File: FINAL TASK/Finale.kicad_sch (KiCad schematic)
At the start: 32 parts, among them J1 SWD Header, P1 USB_C_Plug, SW1 RESET, SW2 BOOT, U1 STM32F103C8T6, U2 AS5048B, U3 AS5048B, U4 AS5048B, U5 AS5048B, U6 AMS1117-3.3, Y1 Crystal

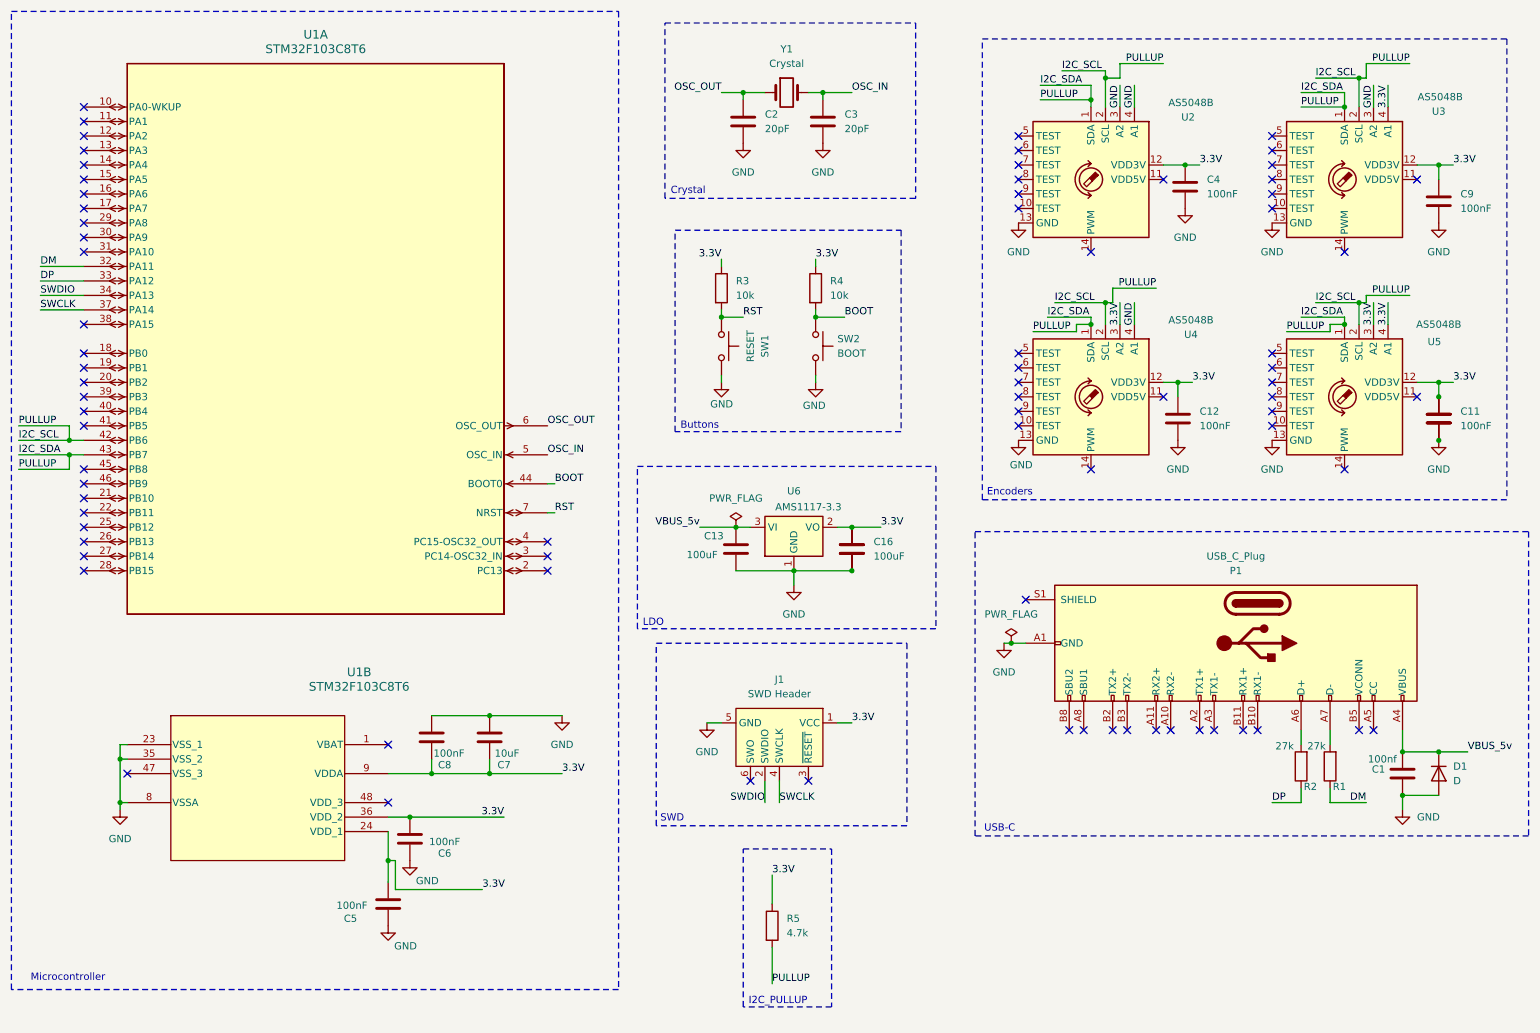
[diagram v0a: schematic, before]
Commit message: Added working directory
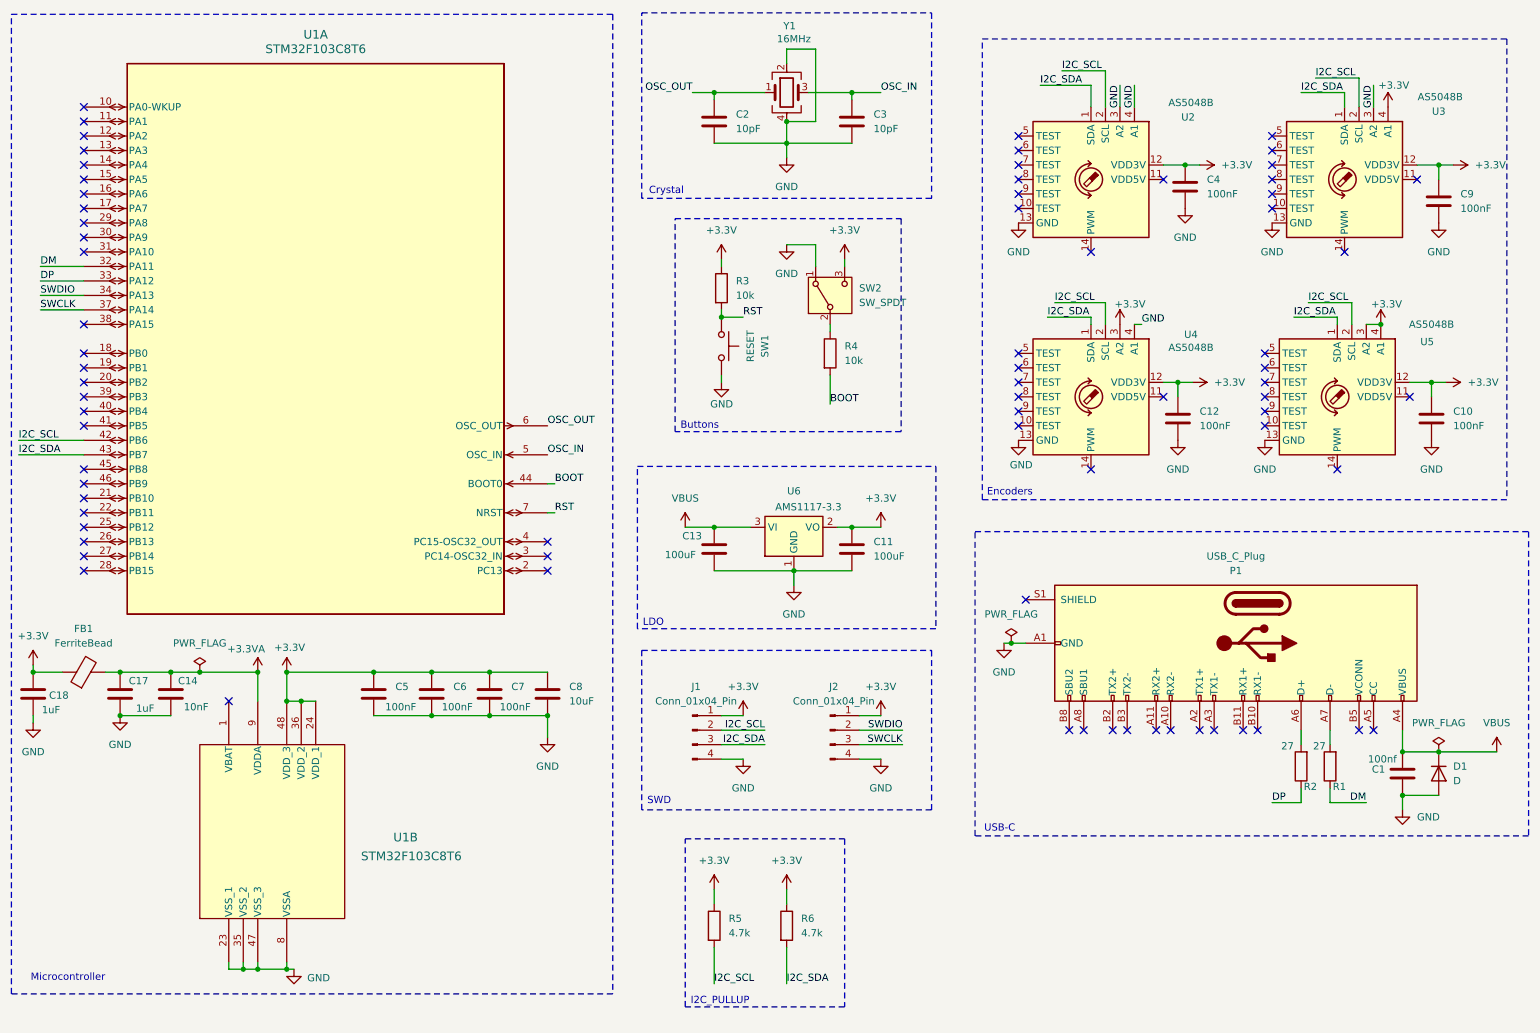
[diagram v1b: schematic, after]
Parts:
- removed C15: 100uF, Capacitor_SMD:C_0805_2012Metric, symbol Device:C
- removed C16: C, Capacitor_SMD:C_0805_2012Metric, symbol Device:C
- removed J1: SWD Header, Connector:Tag-Connect_TC2030-IDC-NL_2x03_P1.27mm_Vertical, symbol Connector:Conn_ARM_SWD_TagConnect_TC2030-NL
- removed SW2: BOOT, Button_Switch_SMD:SW_Push_SPST_NO_Alps_SKRK, symbol Switch:SW_Push
- removed Y1: Crystal, symbol Device:Crystal
- added C14: 10nF, Capacitor_SMD:C_0402_1005Metric, symbol Device:C
- added C17, C18: 1uF, Capacitor_SMD:C_0402_1005Metric, symbol Device:C
- added FB1: FerriteBead, Inductor_SMD:L_0805_2012Metric, symbol Device:FerriteBead
- added J1, J2: Conn_01x04_Pin, Connector_JST:JST_VH_B4P-VH-FB-B_1x04_P3.96mm_Vertical, symbol Connector:Conn_01x04_Pin
- added R6: 4.7k, Resistor_SMD:R_0805_2012Metric, symbol Device:R
- added SW2: SW_SPDT, Button_Switch_SMD:SW_SPDT_CK_JS102011SAQN, symbol Switch:SW_SPDT
- added Y1: 16MHz, Crystal:Crystal_SMD_3225-4Pin_3.2x2.5mm, symbol Device:Crystal_GND24
- C10: value C -> 100nF
- C11: value 100nF -> 100uF
- C2, C3: value 20pF -> 10pF; footprint Capacitor_SMD:C_0805_2012Metric -> Capacitor_SMD:C_0402_1005Metric
- C4, C5, C6: footprint Capacitor_SMD:C_0805_2012Metric -> Capacitor_SMD:C_0402_1005Metric
- C7: value 10uF -> 100nF; footprint Capacitor_SMD:C_0805_2012Metric -> Capacitor_SMD:C_0402_1005Metric
- C8: value 100nF -> 10uF
- R1, R2: value 27k -> 27
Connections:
- net GND: now also C5.2, C6.2, C7.2, C8.2, U1.47 (VSS_3), C14.2, C17.2, C18.2, J1.4 (Pin_4), J2.4 (Pin_4), SW2.1 (A), Y1.2, Y1.4; no longer C5.1, C6.1, C7.1, C8.1
- net I2C_SCL: now also J1.2 (Pin_2); no longer U1.43 (PB7), U2.1 (SDA), U3.1 (SDA), U4.1 (SDA), U5.1 (SDA)
- net OSC_IN: now also Y1.3
- net OSC_OUT: now also Y1.1
- net SWCLK: now also J2.3 (Pin_3)
- net SWDIO: now also J2.2 (Pin_2)
- net +3.3V: now reaches U1.48 (VDD_3)
- net +3.3V: now also C10.1, C11.1, C12.1, C4.1, C5.1, C6.1, C7.1, C8.1, C9.1, R3.1, R5.1, U1.24 (VDD_1), U1.36 (VDD_2), U2.12 (VDD3V), U3.12 (VDD3V), U3.4 (A1), U4.12 (VDD3V), U4.3 (A2), U5.12 (VDD3V), U5.3 (A2), U5.4 (A1), U6.2 (VO), C18.1, FB1.1, J1.1 (Pin_1), J2.1 (Pin_1), R6.1, SW2.3 (C)
- removed net 3.3V: C10.1, C11.1, C12.1, C4.1, C5.2, C6.2, C7.2, C8.2, C9.1, R3.1, R4.1, R5.1, U1.24 (VDD_1), U1.36 (VDD_2), U1.9 (VDDA), U2.12 (VDD3V), U3.12 (VDD3V), U3.4 (A1), U4.12 (VDD3V), U4.3 (A2), U5.12 (VDD3V), U5.3 (A2), U5.4 (A1), U6.2 (VO)
- net VBUS_5v renamed VBUS
- new net: R4.1, SW2.2 (B)
- new net +3.3VA: C14.1, C17.1, FB1.2, U1.9 (VDDA)
- new net I2C_SDA: J1.3 (Pin_3), R6.2, U1.43 (PB7), U2.1 (SDA), U3.1 (SDA), U4.1 (SDA), U5.1 (SDA)
- no-connect marks 79 -> 75
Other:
- moved on the sheet: C13, C2, C3, R4, R5, U1B, U5

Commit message: C
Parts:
- removed C17, C18: 1uF, Capacitor_SMD:C_0402_1005Metric, symbol Device:C
- removed D1: D, Diode_SMD:D_0805_2012Metric, symbol Device:D
- removed FB1: FerriteBead, Inductor_SMD:L_0805_2012Metric, symbol Device:FerriteBead
- removed R1, R2: 27, Resistor_SMD:R_0805_2012Metric, symbol Device:R
- added C15: 100nF, Capacitor_SMD:C_0402_1005Metric, symbol Device:C
- C10, C11, C12, C13, C9: footprint Capacitor_SMD:C_0805_2012Metric -> Capacitor_SMD:C_0402_1005Metric
- C14: value 10nF -> 100nF
- P1: footprint Connector_USB:USB_C_Plug_Molex_105444 -> USB-C:GCT_USB4085-GF-A_REVB
- SW1: footprint Button_Switch_SMD:SW_Push_SPST_NO_Alps_SKRK -> SPST:SW_FSM8JH
- SW2: footprint Button_Switch_SMD:SW_SPDT_CK_JS102011SAQN -> SPDT:SW_MINI-SPDT-SW
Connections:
- net +3.3VA is gone; now on net +3.3V: C14.1, U1.9 (VDDA)
- net +3.3V: now also U1.1 (VBAT), C15.1
- net DM: now also P1.A7 (D-)
- net DP: now also P1.A6 (D+)
- net GND: now also P1.S1 (SHIELD), U2.5 (TEST), U3.5 (TEST), U4.5 (TEST), U5.5 (TEST), C15.2
- no-connect marks 75 -> 69
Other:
- moved on the sheet: C12, C4, C5, C6, C7, C8, U1B, U2, U4

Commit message: Done
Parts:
- added H1, H2, H3, H4: MountingHole, MountingHole:MountingHole_2.1mm, symbol Mechanical:MountingHole
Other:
- note added: "Mounting holes"
- moved on the sheet: R5, R6
